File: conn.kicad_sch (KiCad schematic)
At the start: 5 parts, among them J8 USB_C_Receptacle_USB2.0_16P, U12 SRV05-4

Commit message: PCB schematic design
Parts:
- added J2: Conn_01x04_Pin, symbol Connector:Conn_01x04_Pin
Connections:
- net GND: now also J2.4 (Pin_4)
- new net +3.3V: J2.3 (Pin_3)
- new net IMU_SCL: J2.2 (Pin_2)
- new net IMU_SDA: J2.1 (Pin_1)
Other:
- moved on the sheet: FB1, J8, R27, R28, U12

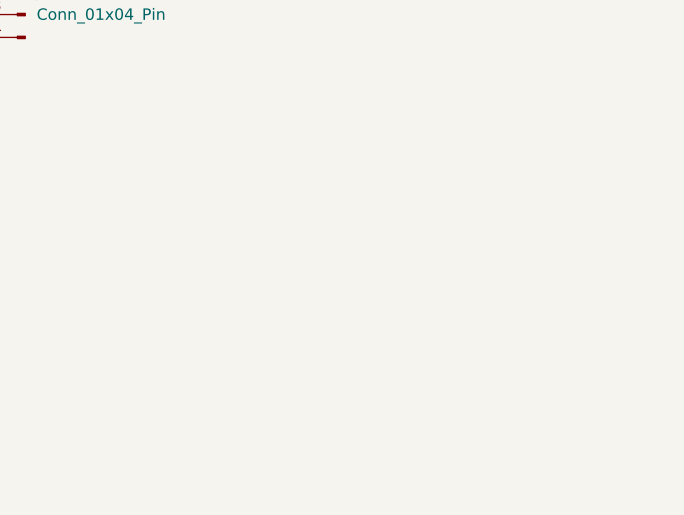
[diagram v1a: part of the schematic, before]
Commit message: Connected hierarchical boards
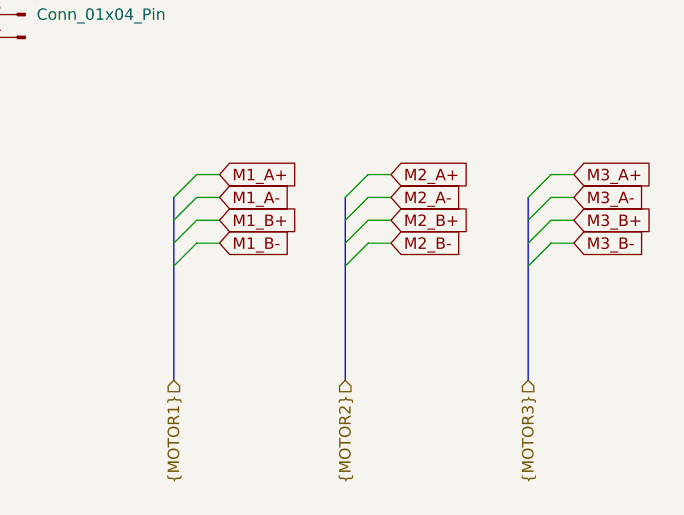
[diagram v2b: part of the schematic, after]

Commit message: Finished design
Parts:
- removed J8: USB_C_Receptacle_USB2.0_16P, Connector_USB:USB_C_Receptacle_GCT_USB4105-xx-A_16P_TopMnt_Horizontal, symbol Connector:USB_C_Receptacle_USB2.0_16P
- added H1, H2, H3, H4: MountingHole_Pad, MountingHole:MountingHole_3.2mm_M3_DIN965_Pad, symbol Mechanical:MountingHole_Pad
- added J2: USB4105GFA, Project_Components:GCT_USB4105GFA, symbol Project_Components:USB4105GFA
- added J3, J4, J5: Conn_01x04_Pin, Connector_JST:JST_XH_B4B-XH-A_1x04_P2.50mm_Vertical, symbol Connector:Conn_01x04_Pin
- added TP1: VBUS, TestPoint:TestPoint_Pad_D1.5mm, symbol Connector:TestPoint
- added TP2: 3V3, TestPoint:TestPoint_Pad_D1.5mm, symbol Connector:TestPoint
- added TP3: VM, TestPoint:TestPoint_Pad_D1.5mm, symbol Connector:TestPoint
- added TP4: BATT, TestPoint:TestPoint_Pad_D1.5mm, symbol Connector:TestPoint
- added TP5: GND, TestPoint:TestPoint_Pad_D1.5mm, symbol Connector:TestPoint
- FB1: footprint Inductor_SMD:L_1206_3216Metric_Pad1.22x1.90mm_HandSolder -> Inductor_SMD:L_0603_1608Metric_Pad1.05x0.95mm_HandSolder
- J1: renamed from J2; footprint (none) -> Connector_PinHeader_2.54mm:PinHeader_1x04_P2.54mm_Vertical
- R14: renamed from R27; footprint Resistor_SMD:R_1206_3216Metric_Pad1.30x1.75mm_HandSolder -> Resistor_SMD:R_0603_1608Metric_Pad0.98x0.95mm_HandSolder
- R15: renamed from R28; footprint Resistor_SMD:R_1206_3216Metric_Pad1.30x1.75mm_HandSolder -> Resistor_SMD:R_0603_1608Metric_Pad0.98x0.95mm_HandSolder
- renumbered U12 to U5
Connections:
- net +3.3V: now also TP2.1
- net GND: now also R14.1, H1.1, H2.1, H3.1, H4.1, J2.A1_B12 (GND), J2.B1_A12 (GND), J2.SH1 (SHELL_GND), J2.SH2 (SHELL_GND), J2.SH3 (SHELL_GND), J2.SH4 (SHELL_GND), TP5.1; no longer R14.2
- net M1_A+: now also J3.1 (Pin_1)
- net M1_A-: now also J3.2 (Pin_2)
- net M1_B+: now also J3.3 (Pin_3)
- net M1_B-: now also J3.4 (Pin_4)
- net M2_A+: now also J4.1 (Pin_1)
- net M2_A-: now also J4.2 (Pin_2)
- net M2_B+: now also J4.3 (Pin_3)
- net M2_B-: now also J4.4 (Pin_4)
- net M3_A+: now also J5.1 (Pin_1)
- net M3_A-: now also J5.2 (Pin_2)
- net M3_B+: now also J5.3 (Pin_3)
- net M3_B-: now also J5.4 (Pin_4)
- net USB_D+: now also J2.A6 (DP1), J2.B6 (DP2)
- net USB_D-: now also J2.A7 (DN1), J2.B7 (DN2)
- net VBUS: now also TP1.1
- net VB: now reaches FB1.1
- net VB: now also J2.A4_B9 (VB), J2.B4_A9 (VB)
- net at R15.1: now also J2.B5 (CC2)
- new net: J2.A5 (CC1), R14.2
- new net +BATT: TP4.1
- new net VM: TP3.1
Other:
- moved on the sheet: FB1, R14, R15, U5

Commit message: Minor tweaks
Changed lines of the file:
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@@
+		(color 0 0 0 0)
+	)
+	(junction
+		(at 72.39 54.61)
+		(diameter 0)
 		(color 0 0 0 0)
 	)
@@
 	(wire
 		(pts
-			(xy 67.31 54.61) (xy 74.93 54.61)
+			(xy 67.31 54.61) (xy 72.39 54.61)
 		)
 		(stroke
@@
 		(pts
 			(xy 67.31 74.93) (xy 71.12 74.93)
+		)
+		(stroke
+			(width 0)
+			(type default)
+		)
+	)
+	(wire
+		(pts
+			(xy 72.39 54.61) (xy 74.93 54.61)
 		)
 		(stroke
@@
 					(unit 1)
 				)
+			)
+		)
+	)
+	(symbol
+		(lib_id "power:PWR_FLAG")
+		(at 72.39 54.61 0)
+		(unit 1)
+		(body_style 1)
+		(exclude_from_sim no)
+		(in_bom yes)
+		(on_board yes)
+		(in_pos_files yes)
+		(dnp no)
+		(fields_autoplaced yes)
+		(property "Reference" "#FLG07"
+			(at 72.39 52.705 0)
+			(hide yes)
+			(show_name no)
+			(do_not_autoplace no)
+			(effects
+				(font
+					(size 1.27 1.27)
+				)
+			)
+		)
+		(property "Value" "PWR_FLAG"
+			(at 72.39 49.53 0)
+			(show_name no)
+			(do_not_autoplace no)
+			(effects
+				(font
+					(size 1.27 1.27)
+				)
+			)
+		)
+		(property "Footprint" ""
+			(at 72.39 54.61 0)
+			(hide yes)
+			(show_name no)
+			(do_not_autoplace no)
+			(effects
+				(font
+					(size 1.27 1.27)
+				)
+			)
+		)
+		(property "Datasheet" ""
+			(at 72.39 54.61 0)
+			(hide yes)
+			(show_name no)
+			(do_not_autoplace no)
+			(effects
+				(font
+					(size 1.27 1.27)
+				)
+			)
+		)
+		(property "Description" "Special symbol for telling ERC where power comes from"
+			(at 72.39 54.61 0)
+			(hide yes)
+			(show_name no)
+			(do_not_autoplace no)
+			(effects
+				(font
+					(size 1.27 1.27)
+				)
+			)
+		)
+		(pin "1"
+		)
+		(instances
+			(project "Orion"
+				(path "/f9e05184-c88b-4a88-ae9c-ab2bdb32be7c/c5103ceb-5325-4a84-a025-9638a412984e/e8cecd96-2ee1-409d-9326-5bbf75b8e536"
+					(reference "#FLG07")
+					(unit 1)
+				)

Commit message: Started troublefixing
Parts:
- renumbered H3 to H2, H2 to H3, R14 to R18, R15 to R19
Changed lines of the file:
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@@
 		(dnp no)
 		(fields_autoplaced yes)
-		(property "Reference" "#PWR027"
+		(property "Reference" "#PWR030"
 			(at 83.82 59.69 0)
 			(hide yes)
@@
 			(project "Orion"
 				(path "/f9e05184-c88b-4a88-ae9c-ab2bdb32be7c/c5103ceb-5325-4a84-a025-9638a412984e/e8cecd96-2ee1-409d-9326-5bbf75b8e536"
-					(reference "#PWR027")
+					(reference "#PWR030")
 					(unit 1)
 				)
@@
 		(dnp no)
 		(fields_autoplaced yes)
-		(property "Reference" "#PWR035"
+		(property "Reference" "#PWR038"
 			(at 157.48 115.57 0)
 			(hide yes)
@@
 			(project "Orion"
 				(path "/f9e05184-c88b-4a88-ae9c-ab2bdb32be7c/c5103ceb-5325-4a84-a025-9638a412984e/e8cecd96-2ee1-409d-9326-5bbf75b8e536"
-					(reference "#PWR035")
+					(reference "#PWR038")
 					(unit 1)
 				)
@@
 		(dnp no)
 		(fields_autoplaced yes)
-		(property "Reference" "#PWR036"
+		(property "Reference" "#PWR041"
 			(at 99.06 137.16 0)
 			(hide yes)
@@
 			(project "Orion"
 				(path "/f9e05184-c88b-4a88-ae9c-ab2bdb32be7c/c5103ceb-5325-4a84-a025-9638a412984e/e8cecd96-2ee1-409d-9326-5bbf75b8e536"
-					(reference "#PWR036")
+					(reference "#PWR041")
 					(unit 1)
 				)
@@
 		(dnp no)
 		(fields_autoplaced yes)
-		(property "Reference" "#FLG07"
+		(property "Reference" "#FLG01"
 			(at 72.39 52.705 0)
 			(hide yes)
@@
 			(project "Orion"
 				(path "/f9e05184-c88b-4a88-ae9c-ab2bdb32be7c/c5103ceb-5325-4a84-a025-9638a412984e/e8cecd96-2ee1-409d-9326-5bbf75b8e536"
-					(reference "#FLG07")
+					(reference "#FLG01")
 					(unit 1)
 				)
@@
 		(dnp no)
 		(fields_autoplaced yes)
-		(property "Reference" "#PWR084"
+		(property "Reference" "#PWR043"
 			(at 195.58 151.13 0)
 			(hide yes)
@@
 			(project "Orion"
 				(path "/f9e05184-c88b-4a88-ae9c-ab2bdb32be7c/c5103ceb-5325-4a84-a025-9638a412984e/e8cecd96-2ee1-409d-9326-5bbf75b8e536"
-					(reference "#PWR084")
+					(reference "#PWR043")
 					(unit 1)
 				)
@@
 		(dnp no)
 		(fields_autoplaced yes)
-		(property "Reference" "#PWR031"
+		(property "Reference" "#PWR034"
 			(at 80.01 74.93 0)
 			(hide yes)
@@
 			(project "Orion"
 				(path "/f9e05184-c88b-4a88-ae9c-ab2bdb32be7c/c5103ceb-5325-4a84-a025-9638a412984e/e8cecd96-2ee1-409d-9326-5bbf75b8e536"
-					(reference "#PWR031")
+					(reference "#PWR034")
 					(unit 1)
 				)
@@
 		(dnp no)
 		(fields_autoplaced yes)
-		(property "Reference" "#PWR028"
+		(property "Reference" "#PWR031"
 			(at 138.43 64.77 0)
 			(hide yes)
@@
 			(project "Orion"
 				(path "/f9e05184-c88b-4a88-ae9c-ab2bdb32be7c/c5103ceb-5325-4a84-a025-9638a412984e/e8cecd96-2ee1-409d-9326-5bbf75b8e536"
-					(reference "#PWR028")
+					(reference "#PWR031")
 					(unit 1)
 				)
@@
 		(dnp no)
 		(fields_autoplaced yes)
-		(property "Reference" "#PWR032"
+		(property "Reference" "#PWR035"
 			(at 138.43 92.71 0)
 			(hide yes)
@@
 			(project "Orion"
 				(path "/f9e05184-c88b-4a88-ae9c-ab2bdb32be7c/c5103ceb-5325-4a84-a025-9638a412984e/e8cecd96-2ee1-409d-9326-5bbf75b8e536"
-					(reference "#PWR032")
+					(reference "#PWR035")
 					(unit 1)
 				)
@@
 		(dnp no)
 		(fields_autoplaced yes)
-		(property "Reference" "#PWR037"
+		(property "Reference" "#PWR042"
 			(at 128.27 147.32 0)
 			(hide yes)
@@
 			(project "Orion"
 				(path "/f9e05184-c88b-4a88-ae9c-ab2bdb32be7c/c5103ceb-5325-4a84-a025-9638a412984e/e8cecd96-2ee1-409d-9326-5bbf75b8e536"
-					(reference "#PWR037")
+					(reference "#PWR042")
 					(unit 1)
 				)
@@
 		(dnp no)
 		(fields_autoplaced yes)
-		(property "Reference" "#PWR083"
+		(property "Reference" "#PWR044"
 			(at 219.71 151.13 0)
 			(hide yes)
@@
 			(project "Orion"
 				(path "/f9e05184-c88b-4a88-ae9c-ab2bdb32be7c/c5103ceb-5325-4a84-a025-9638a412984e/e8cecd96-2ee1-409d-9326-5bbf75b8e536"
-					(reference "#PWR083")
+					(reference "#PWR044")
 					(unit 1)
 				)
@@
 		(dnp no)
 		(fields_autoplaced yes)
-		(property "Reference" "#PWR025"
+		(property "Reference" "#PWR028"
 			(at 87.63 54.61 0)
 			(hide yes)
@@
 			(project "Orion"
 				(path "/f9e05184-c88b-4a88-ae9c-ab2bdb32be7c/c5103ceb-5325-4a84-a025-9638a412984e/e8cecd96-2ee1-409d-9326-5bbf75b8e536"
-					(reference "#PWR025")
+					(reference "#PWR028")
 					(unit 1)
 				)
@@
 		(dnp no)
 		(fields_autoplaced yes)
-		(property "Reference" "#PWR081"
+		(property "Reference" "#PWR039"
 			(at 195.58 142.24 0)
 			(hide yes)
@@
 			(project "Orion"
 				(path "/f9e05184-c88b-4a88-ae9c-ab2bdb32be7c/c5103ceb-5325-4a84-a025-9638a412984e/e8cecd96-2ee1-409d-9326-5bbf75b8e536"
-					(reference "#PWR081")
+					(reference "#PWR039")
 					(unit 1)
 				)
@@
 		(dnp no)
 		(fields_autoplaced yes)
-		(property "Reference" "#PWR029"
+		(property "Reference" "#PWR032"
 			(at 191.77 63.5 0)
 			(hide yes)
@@
 			(project "Orion"
 				(path "/f9e05184-c88b-4a88-ae9c-ab2bdb32be7c/c5103ceb-5325-4a84-a025-9638a412984e/e8cecd96-2ee1-409d-9326-5bbf75b8e536"
-					(reference "#PWR029")
+					(reference "#PWR032")
 					(unit 1)
 				)
@@
 		(dnp no)
 		(fields_autoplaced yes)
-		(property "Reference" "#PWR034"
+		(property "Reference" "#PWR037"
 			(at 128.27 115.57 0)
 			(hide yes)
@@
 			(project "Orion"
 				(path "/f9e05184-c88b-4a88-ae9c-ab2bdb32be7c/c5103ceb-5325-4a84-a025-9638a412984e/e8cecd96-2ee1-409d-9326-5bbf75b8e536"
-					(reference "#PWR034")
+					(reference "#PWR037")
 					(unit 1)
 				)
@@
 		(dnp no)
 		(fields_autoplaced yes)
-		(property "Reference" "H2"
+		(property "Reference" "H3"
 			(at 198.12 139.6999 0)
 			(show_name no)
@@
 			(project "Orion"
 				(path "/f9e05184-c88b-4a88-ae9c-ab2bdb32be7c/c5103ceb-5325-4a84-a025-9638a412984e/e8cecd96-2ee1-409d-9326-5bbf75b8e536"
-					(reference "H2")
+					(reference "H3")
 					(unit 1)
 				)
@@
 		(dnp no)
 		(fields_autoplaced yes)
-		(property "Reference" "H3"
+		(property "Reference" "H2"
 			(at 222.25 130.8099 0)
 			(show_name no)
@@
 			(project "Orion"
 				(path "/f9e05184-c88b-4a88-ae9c-ab2bdb32be7c/c5103ceb-5325-4a84-a025-9638a412984e/e8cecd96-2ee1-409d-9326-5bbf75b8e536"
-					(reference "H3")
+					(reference "H2")
 					(unit 1)
 				)
@@
 		(dnp no)
 		(fields_autoplaced yes)
-		(property "Reference" "#PWR082"
+		(property "Reference" "#PWR040"
 			(at 219.71 142.24 0)
 			(hide yes)
@@
 			(project "Orion"
 				(path "/f9e05184-c88b-4a88-ae9c-ab2bdb32be7c/c5103ceb-5325-4a84-a025-9638a412984e/e8cecd96-2ee1-409d-9326-5bbf75b8e536"
-					(reference "#PWR082")
+					(reference "#PWR040")
 					(unit 1)
 				)
@@
 		(dnp no)
 		(fields_autoplaced yes)
-		(property "Reference" "#PWR030"
+		(property "Reference" "#PWR033"
 			(at 181.61 66.04 0)
 			(hide yes)
@@
 			(project "Orion"
 				(path "/f9e05184-c88b-4a88-ae9c-ab2bdb32be7c/c5103ceb-5325-4a84-a025-9638a412984e/e8cecd96-2ee1-409d-9326-5bbf75b8e536"
-					(reference "#PWR030")
+					(reference "#PWR033")
 					(unit 1)
 				)
@@
 		(in_pos_files yes)
 		(dnp no)
-		(property "Reference" "R14"
+		(property "Reference" "R18"
 			(at 21.59 59.69 90)
 			(show_name no)
@@
 			(project "Orion"
 				(path "/f9e05184-c88b-4a88-ae9c-ab2bdb32be7c/c5103ceb-5325-4a84-a025-9638a412984e/e8cecd96-2ee1-409d-9326-5bbf75b8e536"
-					(reference "R14")
+					(reference "R18")
 					(unit 1)
 				)
@@
 		(in_pos_files yes)
 		(dnp no)
-		(property "Reference" "R15"
+		(property "Reference" "R19"
 			(at 72.39 59.69 90)
 			(show_name no)
@@
 			(project "Orion"
 				(path "/f9e05184-c88b-4a88-ae9c-ab2bdb32be7c/c5103ceb-5325-4a84-a025-9638a412984e/e8cecd96-2ee1-409d-9326-5bbf75b8e536"
-					(reference "R15")
+					(reference "R19")
 					(unit 1)
 				)
@@
 		(dnp no)
 		(fields_autoplaced yes)
-		(property "Reference" "#PWR033"
+		(property "Reference" "#PWR036"
 			(at 99.06 115.57 0)
 			(hide yes)
@@
 			(project "Orion"
 				(path "/f9e05184-c88b-4a88-ae9c-ab2bdb32be7c/c5103ceb-5325-4a84-a025-9638a412984e/e8cecd96-2ee1-409d-9326-5bbf75b8e536"
-					(reference "#PWR033")
+					(reference "#PWR036")
 					(unit 1)
 				)
@@
 		(dnp no)
 		(fields_autoplaced yes)
-		(property "Reference" "#PWR026"
+		(property "Reference" "#PWR029"
 			(at 10.16 59.69 0)
 			(hide yes)
@@
 			(project "Orion"
 				(path "/f9e05184-c88b-4a88-ae9c-ab2bdb32be7c/c5103ceb-5325-4a84-a025-9638a412984e/e8cecd96-2ee1-409d-9326-5bbf75b8e536"
-					(reference "#PWR026")
+					(reference "#PWR029")
 					(unit 1)
 				)

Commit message: Started rerouting changes
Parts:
- renumbered R18 to R14, R19 to R15
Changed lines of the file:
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@@
 		(in_pos_files yes)
 		(dnp no)
-		(property "Reference" "R18"
+		(property "Reference" "R14"
 			(at 21.59 59.69 90)
 			(show_name no)
@@
 			(project "Orion"
 				(path "/f9e05184-c88b-4a88-ae9c-ab2bdb32be7c/c5103ceb-5325-4a84-a025-9638a412984e/e8cecd96-2ee1-409d-9326-5bbf75b8e536"
-					(reference "R18")
+					(reference "R14")
 					(unit 1)
 				)
@@
 		(in_pos_files yes)
 		(dnp no)
-		(property "Reference" "R19"
+		(property "Reference" "R15"
 			(at 72.39 59.69 90)
 			(show_name no)
@@
 			(project "Orion"
 				(path "/f9e05184-c88b-4a88-ae9c-ab2bdb32be7c/c5103ceb-5325-4a84-a025-9638a412984e/e8cecd96-2ee1-409d-9326-5bbf75b8e536"
-					(reference "R19")
+					(reference "R15")
 					(unit 1)
 				)
